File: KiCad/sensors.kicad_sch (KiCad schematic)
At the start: 0 parts

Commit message: feat: add IMU low G
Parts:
- added C34, C35, C36: 100nF, ODB:C_0402_1005Metric, symbol Device:C_Small
- added C51: 1uF, Capacitor_SMD:C_0603_1608Metric, symbol Device:C_Small
- added R49, R50: 10k, Resistor_SMD:R_0603_1608Metric, symbol Device:R
- added R82, R83: 5k 1%, Resistor_SMD:R_0603_1608Metric, symbol Device:R
- added U2: BNO055, QFN_BNO055_BOS, symbol PayloadLibrary:BNO055
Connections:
- new net: R49.2, U2.4 (NBOOT_LOAD_PIN)
- new net: C51.1, U2.9 (CAP)
- new net +3V3: C34.1, C35.2, C36.1, R49.1, R50.1, R82.1, R83.1, U2.28 (VDDIO), U2.3 (VDD), U2.5 (PS1)
- new net GND: C34.2, C35.1, C36.2, C51.2, U2.17 (COM3), U2.18 (COM2), U2.2 (GND), U2.25 (GNDIO), U2.6 (PS0)
- new net IMU_I2C1_SCL: R82.2, U2.19 (COM1)
- new net IMU_I2C1_SDA: R83.2, U2.20 (COM0)
- new net IMU_INT: U2.14 (INT)
- new net IMU_nRESET: R50.2, U2.11 (NRESET)
- no-connect marks 0 -> 14
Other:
- note added: "Active low"
- note added: "Addess selection 0x28"
- note added: "Digital OUT"
- note added: "IMU Low G"
- note added: "Max consumption 12.3mA"
- note added: "OSC (optional)"
- note added: "Pull-up"
- note added: "SCL"
- note added: "SDA"
- note added: "Use internal crystal"

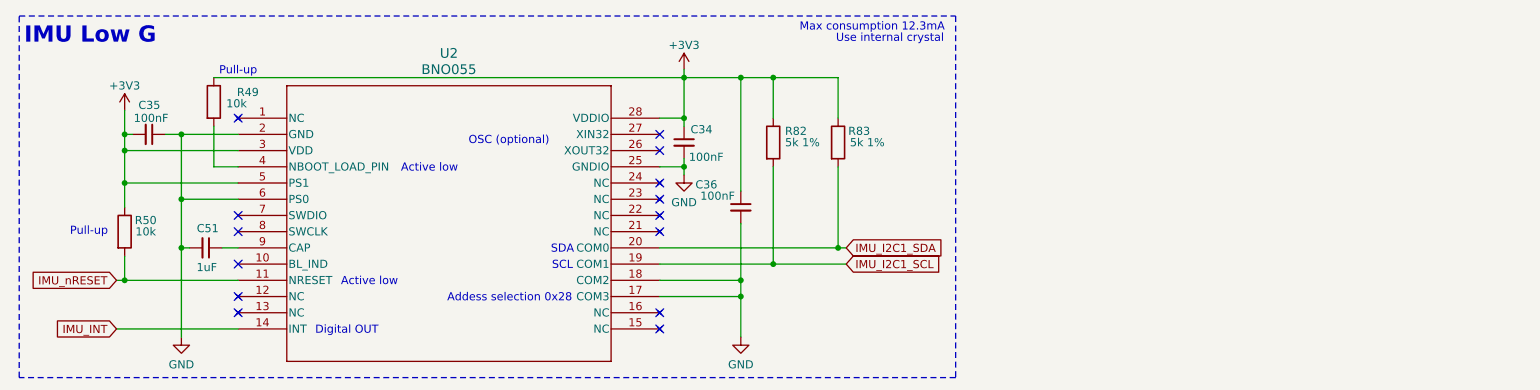
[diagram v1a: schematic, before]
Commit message: Added Temperature sensor
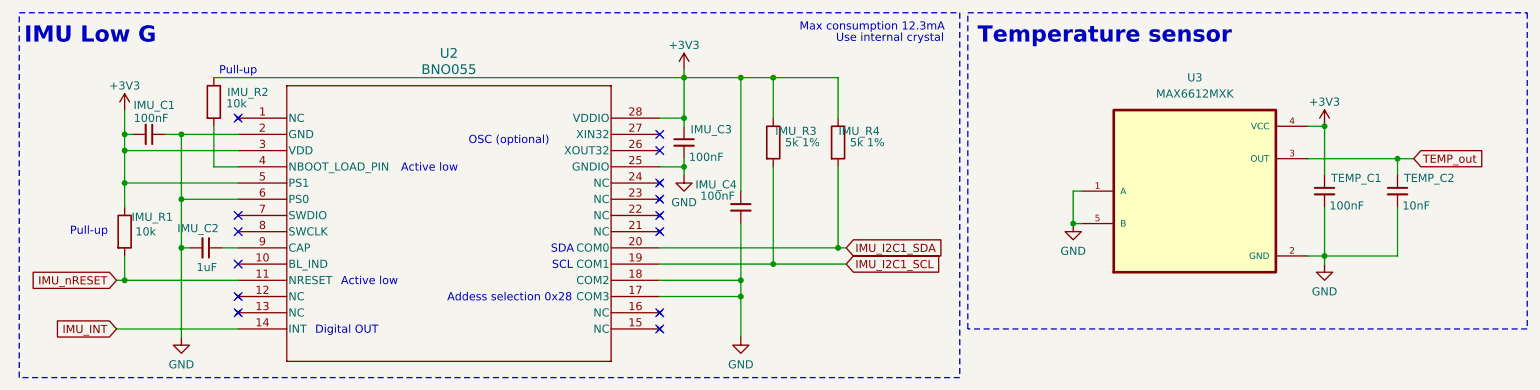
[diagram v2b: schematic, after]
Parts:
- added TEMP_C1: 100nF, ODB:C_0402_1005Metric, symbol Device:C_Small
- added TEMP_C2: 10nF, ODB:C_0402_1005Metric, symbol Device:C_Small
- added U3: MAX6612MXK, MAX6612MXK:SOT65P210X110-5N, symbol PayloadLibrary:MAX6612MXK
- renumbered C35 to IMU_C1, C51 to IMU_C2, C34 to IMU_C3, C36 to IMU_C4, R50 to IMU_R1, R49 to IMU_R2, R82 to IMU_R3, R83 to IMU_R4
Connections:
- net +3V3: now also TEMP_C1.1, U3.4 (VCC)
- net GND: now also TEMP_C1.2, TEMP_C2.2, U3.1 (A), U3.2 (GND), U3.5 (B)
- new net TEMP_out: TEMP_C2.1, U3.3 (OUT)
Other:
- note added: "Temperature sensor"

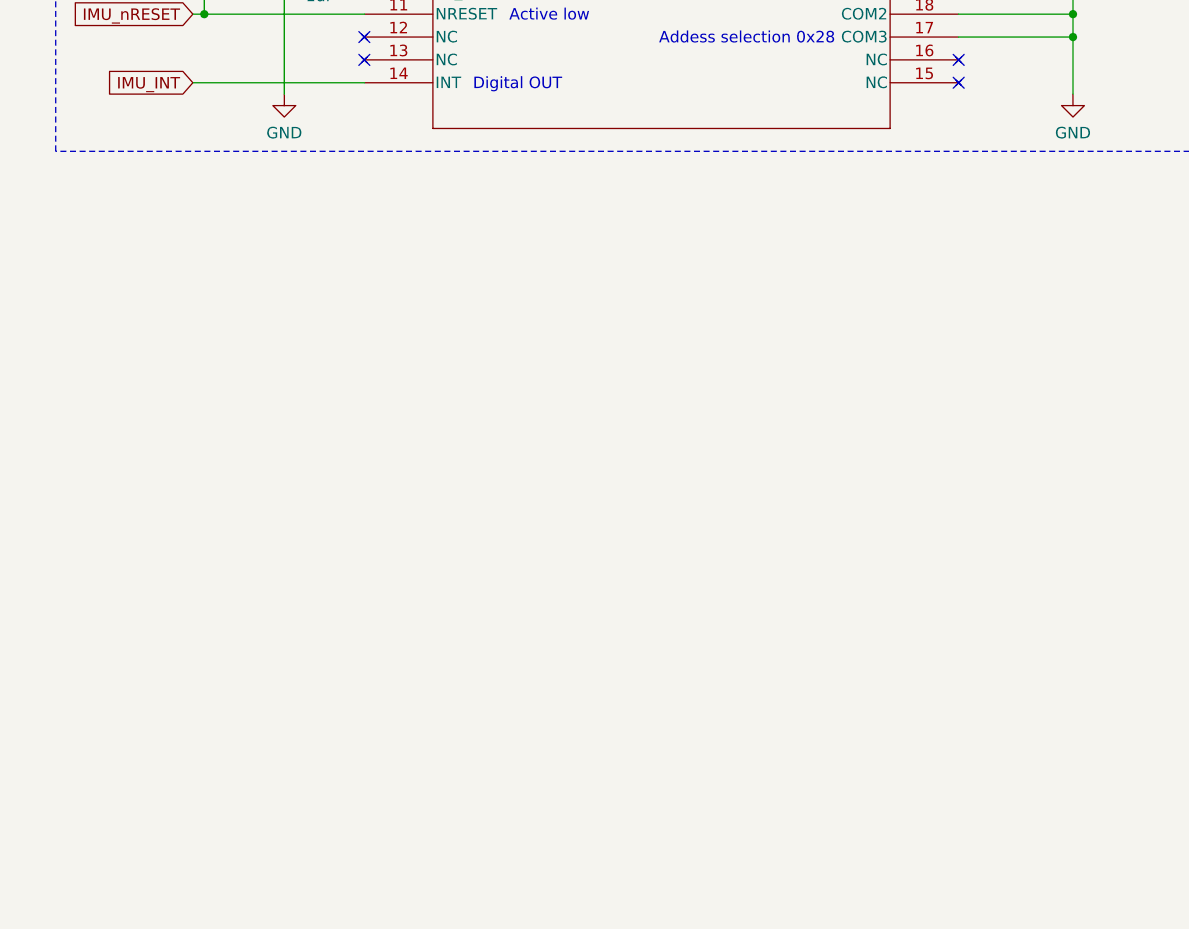
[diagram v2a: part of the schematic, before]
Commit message: feat: add sd + gps+ swd + LED RG + add sma
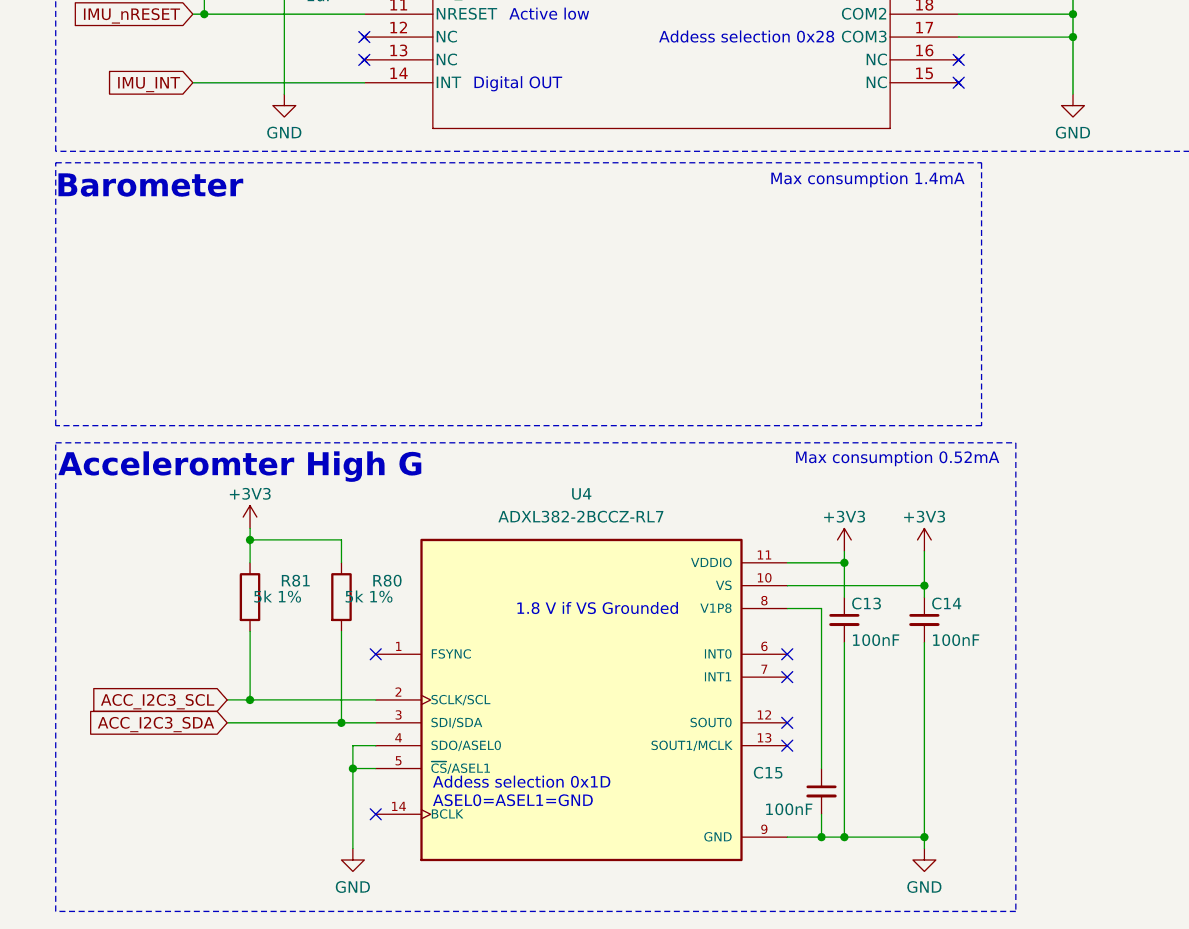
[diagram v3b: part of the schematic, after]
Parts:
- added C13, C14, C15: 100nF, ODB:C_0402_1005Metric, symbol Device:C_Small
- added R80, R81: 5k 1%, Resistor_SMD:R_0603_1608Metric, symbol Device:R
- added U4: ADXL382-2BCCZ-RL7, ADXL382-2BCCZ-RL7:XDCR_ADXL382-2BCCZ-RL7, symbol PayloadLibrary:ADXL382-2BCCZ-RL7
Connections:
- net +3V3: now also C13.1, C14.1, R80.1, R81.1, U4.10 (VS), U4.11 (VDDIO)
- net GND: now also C13.2, C14.2, C15.2, U4.4 (SDO/ASEL0), U4.5 (~{CS}/ASEL1), U4.9 (GND)
- new net: C15.1, U4.8 (V1P8)
- new net ACC_I2C3_SCL: R81.2, U4.2 (SCLK/SCL)
- new net ACC_I2C3_SDA: R80.2, U4.3 (SDI/SDA)
- no-connect marks 14 -> 20
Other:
- note added: "1.8 V if VS Grounded"
- note added: "Acceleromter High G"
- note added: "Addess selection 0x1D ASEL0=ASEL1=GND"
- note added: "Barometer"
- note added: "Max consumption 0.52mA"
- note added: "Max consumption 1.4mA"

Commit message: Added hardware
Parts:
- added A1: MS583702BA01-50, MS583702BA01-50:XDCR_MS583702BA01-50, symbol PayloadLibrary:MS583702BA01-50
- added BAR_C1, GPS_C1: 100nF, ODB:C_0402_1005Metric, symbol Device:C_Small
- added GPS_L1: 100nH, Inductor_SMD:L_0603_1608Metric, symbol Device:L
- added GPS_R1: 10k, Resistor_SMD:R_0603_1608Metric, symbol Device:R
- added GPS_R2: 10R, ODB:R_0402_1005Metric, symbol Device:R
- added J1: SMA-50G, CONN_142-0701-801, symbol PayloadLibrary:SMA-50G
- added U5: L76L-M33, L76L-M33:XCVR_L76L-M33, symbol PayloadLibrary:L76L-M33
- renumbered C13 to ACCEL_C1, C14 to ACCEL_C2, C15 to ACCEL_C3, R81 to ACCEL_R1, R80 to ACCEL_R2
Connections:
- net +3V3: now also A1.2 (VDD), BAR_C1.1, GPS_C1.1, GPS_R1.1, U5.6 (V_BCKP), U5.8 (VCC)
- net GND: now also A1.1 (GND), BAR_C1.2, GPS_C1.2, GPS_R1.2, J1.2 (SHIELD), J1.3 (SHIELD), J1.4 (SHIELD), J1.5 (SHIELD), U5.1 (GND), U5.10 (GND__1), U5.12 (GND__2), U5.9 (RESET)
- net ACC_I2C3_SCL renamed ACCEL_I2C_SCL
- net ACC_I2C3_SDA renamed ACCEL_I2C_SDA
- net IMU_I2C1_SCL renamed IMU_I2C_SCL
- net IMU_I2C1_SDA renamed IMU_I2C_SDA
- new net: GPS_L1.1, GPS_R2.1
- new net: GPS_R2.2, U5.14 (VCC_RF)
- new net BAR_I2C_SCL: A1.3 (SCL)
- new net BAR_I2C_SDA: A1.4 (SDA)
- new net GPS_USART_RX: U5.2 (TXD1)
- new net GPS_USART_TX: U5.3 (RXD1)
- new net L76LM33_RF: GPS_L1.2, J1.1, U5.11 (RF_IN)
- no-connect marks 20 -> 24
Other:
- note added: "GPS"
- note added: "Max consumption ~50mA"
- note removed: "Max consumption 1.4mA"
